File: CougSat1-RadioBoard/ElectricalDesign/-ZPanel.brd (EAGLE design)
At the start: 96 x 96 mm, 46 parts, among them J1 High Gain Antenna, J2 Deployables, J3 High Gain +, J4 ADCS, J5 Flap +X, J6 Flap -X, J7 Flap +Y, J8 Flap -Y, U1 AD7291, U3 AD8515

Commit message: Layout 1.0.2
Ready for RF
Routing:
- net AGND: track 314.9 -> 315.8 mm

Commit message: Laid out RF
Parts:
- moved J6 104.7 mm to (-26.0, 0.00)
- moved J8 104.7 mm to (0.00, -26.0)
- moved J1 69.2 mm to (16.0, -23.3), turned to 90 degrees
- moved C1 68.2 mm to (-42.1, 1.56)
- moved C11 68.2 mm to (-36.0, 11.6)
- moved C12 68.2 mm to (-17.8, 23.6)
- moved C2 68.2 mm to (-35.2, 19.5)
- moved C3 68.2 mm to (-35.9, 15.6)
- moved C4 68.2 mm to (-7.68, 42.0)
- moved C5 68.2 mm to (-17.5, 39.6)
- moved C6 68.2 mm to (-41.7, -5.36)
- moved C7 68.2 mm to (-42.5, 7.64)
- moved C8 68.2 mm to (-42.4, 13.6)
- moved C9 68.2 mm to (-26.2, 26.6)
- moved D1 68.2 mm to (-10.3, 33.5)
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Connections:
- net HIGH_G_1 renamed COAX_CENTER
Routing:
- net SPRING_CONTACT: track 136.1 -> 0.00 mm
- net DEPLOY-H: track 99.0 -> 0.00 mm
- net THERM-5: track 115.6 -> 82.6 mm
- net COAX_CENTER: track 0.00 -> 27.8 mm
- net PGND: track 126.2 -> 106.7 mm, vias 0 -> 1
- net DGND: track 60.5 -> 73.6 mm
- net 3.3V: track 48.1 -> 56.0 mm
- net CHASSIS: track 234.3 -> 236.5 mm
- added copper zone on layer 1, net RFGND
- added copper zone on layer 16, net RFGND
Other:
- outline, holes or cut-outs redrawn

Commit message: Update -ZPanel.brd
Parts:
- moved D1 20.6 mm to (8.72, 25.5), turned to 270 degrees
- moved R11 8.60 mm to (-42.4, 9.45)
- moved RN2 8.06 mm to (15.1, 22.6)
- moved RN1 6.71 mm to (20.2, 39.6)
- moved RT2 6.40 mm to (-30.8, -3.55)
- moved C11 6.32 mm to (-42.0, 13.6)
- moved C9 6.32 mm to (-32.2, 28.6)
- moved C3 6.08 mm to (-41.9, 16.6)
- moved R12 5.39 mm to (-4.17, 31.4), flipped to the bottom, turned to 270 degrees
- moved RT4 5.39 mm to (10.6, 18.4)
- moved U3 5.39 mm to (-15.9, 25.5)
- moved C2 5.10 mm to (-40.2, 20.5)
- moved C12 4.12 mm to (-21.8, 22.6)
- moved R3 4.12 mm to (-22.4, 39.6)
- moved C6 3.55 mm to (-45.0, -4.06)
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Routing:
- net SPRING_CONTACT: track 0.00 -> 125.3 mm, vias 0 -> 2
- net DEPLOY-H: track 0.00 -> 90.4 mm, vias 0 -> 2
- net THERM-5: track 82.6 -> 126.6 mm, vias 2 -> 4
- net I2C_SCL_ADCS: track 0.00 -> 43.8 mm, vias 0 -> 1
- net AVDD: track 68.3 -> 104.8 mm, vias 0 -> 4
- net I2C_SDA_ADCS: track 0.00 -> 34.7 mm, vias 0 -> 1
- net PGND: track 106.7 -> 141.3 mm, vias 1 -> 0
- net AGND: track 315.8 -> 344.7 mm, vias 0 -> 1
- net THERM-6: track 95.0 -> 113.2 mm, vias 2 -> 5
- net THERM-1: track 91.7 -> 109.6 mm, vias 2 -> 4
- net THERM-0: track 94.6 -> 111.7 mm
- net THERM-4: track 72.5 -> 88.1 mm, vias 2 -> 4
- net PHOTODIODE_ADC: track 28.5 -> 41.0 mm
- net AVREF: track 54.0 -> 65.7 mm, vias 2 -> 3
- net THERM-3: track 43.4 -> 53.6 mm, vias 2 -> 1
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
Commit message: Ready for review
Ripped up RF traces
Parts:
- removed J1: High Gain Antenna, CougsInSpace-Connectors:U.FL
- removed J2: Deployables, CougsInSpace-Connectors:PICOLOCK1.5-04
- removed J3: High Gain +, CougsInSpace-Connectors:THT-1.0
- removed J5: Flap +X, CougsInSpace-Connectors:SPRING-0990
- removed J6: Flap -X, CougsInSpace-Connectors:SPRING-0990
- removed J7: Flap +Y, CougsInSpace-Connectors:SPRING-0990
- removed J8: Flap -Y, CougsInSpace-Connectors:SPRING-0990
- removed R1, R2: 15Ω 5%, CougsInSpace-Resistors:THT-15MM
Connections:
- removed net COAX_CENTER: J1.CENTER, J3.1
- removed net DEPLOY-H: J2.1, J2.2, R1.1, R2.1
- removed net RFGND: J1.SHIELD@1, J1.SHIELD@13, J1.SHIELD@2
- removed net SPRING_CONTACT: J2.3, J5.1, J6.1, J7.1, J8.1
- net PGND: no longer J2.4, R1.2, R2.2
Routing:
- net SPRING_CONTACT: track 125.3 -> 0.00 mm, vias 2 -> 0
- net PGND: track 141.3 -> 22.8 mm
- net CHASSIS: track 237.0 -> 330.5 mm
- net DEPLOY-H: track 90.4 -> 0.00 mm, vias 2 -> 0
- net COAX_CENTER: track 27.8 -> 0.00 mm
- removed copper zone on layer 1, net RFGND
- removed copper zone on layer 16, net RFGND

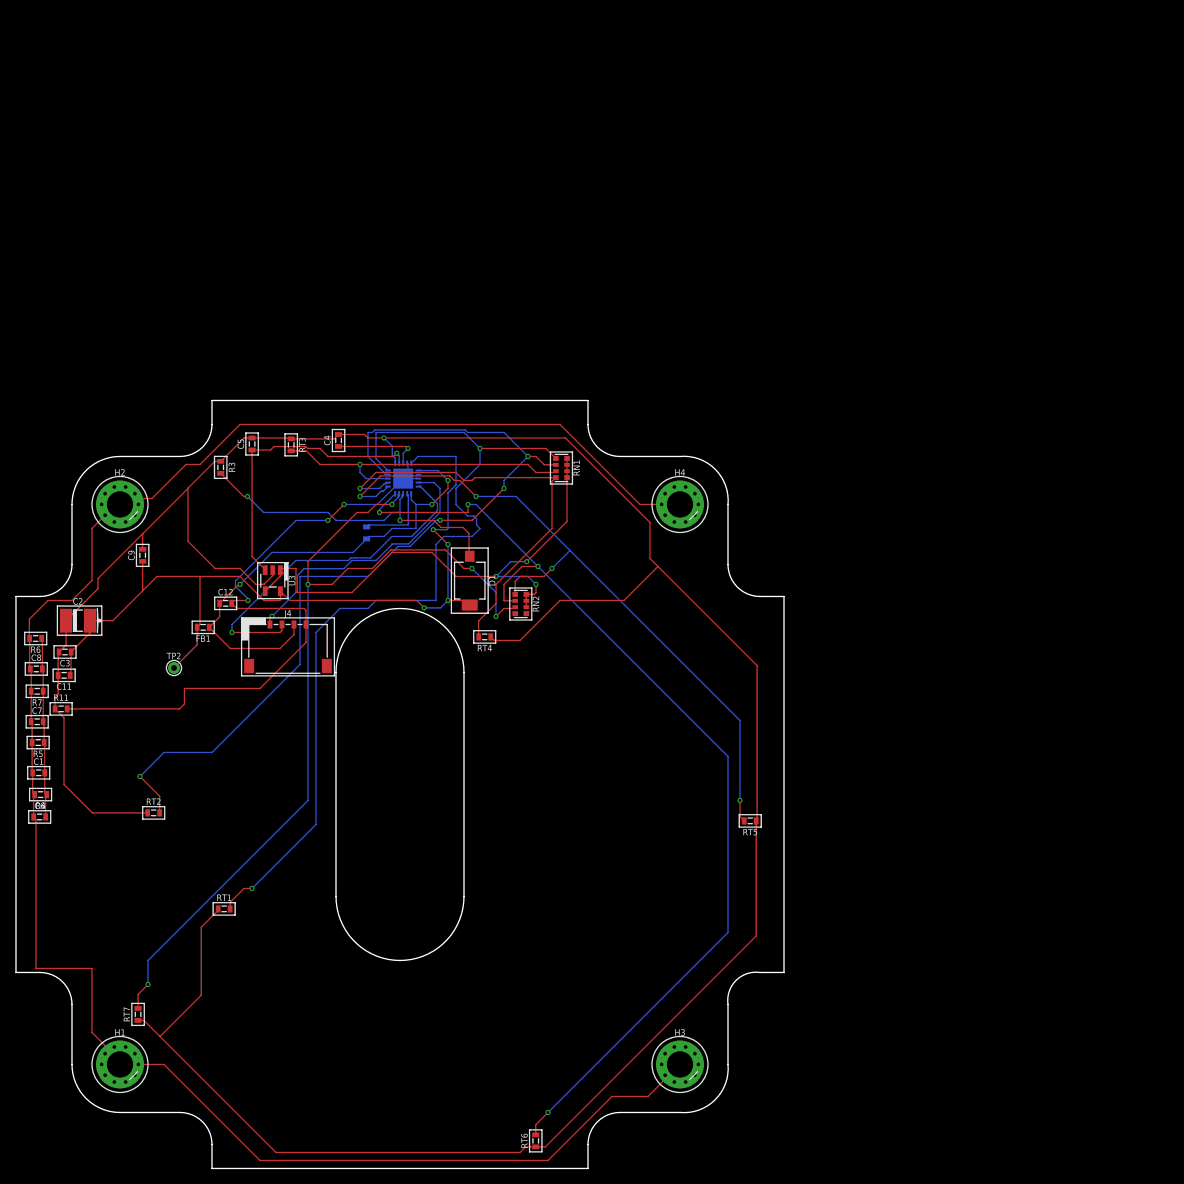
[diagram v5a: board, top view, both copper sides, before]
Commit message: Update -Z Layout
Layout updated considering these notes
- Caps and for chassis should be placed near contacts
- avoid sharp corners
- distance inconsistencies
- top layer components
- snap everything to the grid 0.25mm grid
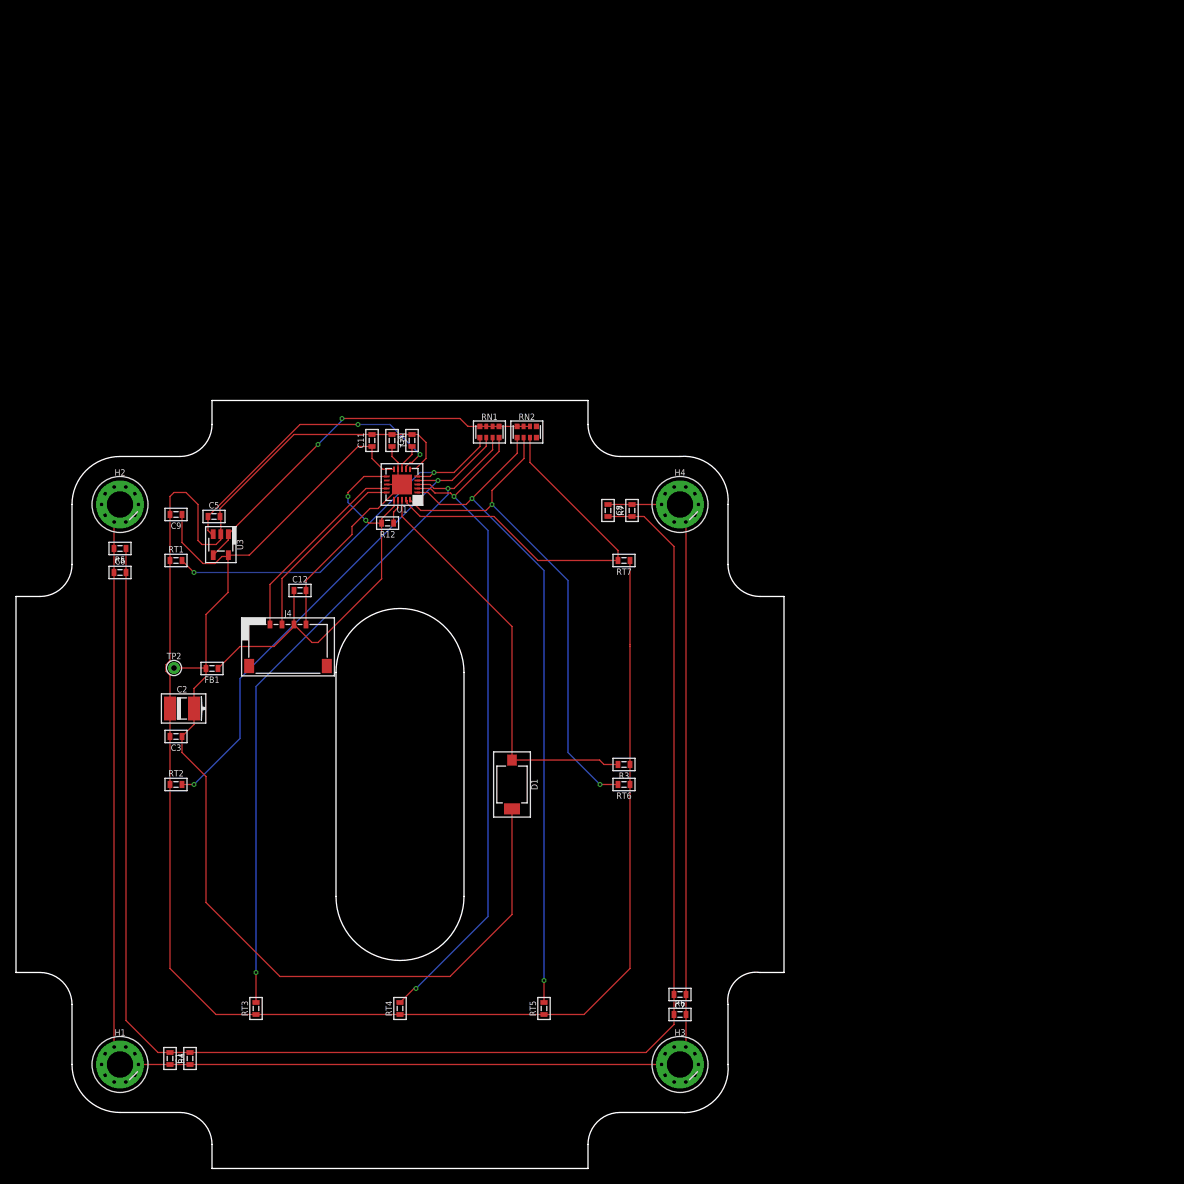
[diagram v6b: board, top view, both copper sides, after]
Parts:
- moved R6 93.3 mm to (35.0, -28.8), turned to 0 degrees
- moved C7 87.3 mm to (35.0, -26.2), turned to 180 degrees
- moved RT7 83.1 mm to (28.0, 28.0), turned to 180 degrees
- moved R7 77.7 mm to (29.0, 34.2), turned to 90 degrees
- moved C8 74.2 mm to (26.0, 34.2), turned to 270 degrees
- moved RT3 70.6 mm to (-18.0, -28.0), turned to 90 degrees
- moved R3 62.6 mm to (28.0, 2.50), turned to 180 degrees
- moved R11 53.3 mm to (-1.00, 43.0), turned to 270 degrees
- moved C11 48.4 mm to (-3.50, 43.0), turned to 90 degrees
- moved RT4 47.6 mm to (0.00, -28.0), turned to 90 degrees
- moved RT6 45.9 mm to (28.0, 0.00), turned to 180 degrees
- moved RT1 44.0 mm to (-28.0, 28.0)
- moved C1 40.4 mm to (-26.2, -34.2), turned to 90 degrees
- moved R4 36.7 mm to (-28.8, -34.2), turned to 270 degrees
- moved RT5 34.8 mm to (18.0, -28.0), turned to 90 degrees
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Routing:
- net PGND: track 22.8 -> 200.2 mm
- net AGND: track 344.7 -> 223.3 mm, vias 1 -> 0
- net THERM-0: track 111.7 -> 47.8 mm
- net THERM-6: track 113.2 -> 49.7 mm, vias 5 -> 0
- net THERM-5: track 126.6 -> 64.0 mm, vias 4 -> 2
- net DGND: track 83.5 -> 30.2 mm, vias 3 -> 0
- net THERM-2: track 39.1 -> 87.4 mm, vias 1 -> 2
- net THERM-1: track 109.6 -> 63.6 mm, vias 4 -> 2
- net AVDD: track 104.9 -> 148.8 mm, vias 4 -> 0
- net THERM-3: track 53.6 -> 84.4 mm, vias 1 -> 2
- net CHASSIS: track 330.5 -> 306.2 mm
- net I2C_SCL_ADCS: track 43.8 -> 23.3 mm, vias 1 -> 0
- net AVREF: track 65.7 -> 47.7 mm, vias 3 -> 2
- net PHOTODIODE_ADC: track 41.0 -> 51.7 mm, vias 2 -> 0
- net I2C_SDA_ADCS: track 34.7 -> 24.6 mm, vias 1 -> 0
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
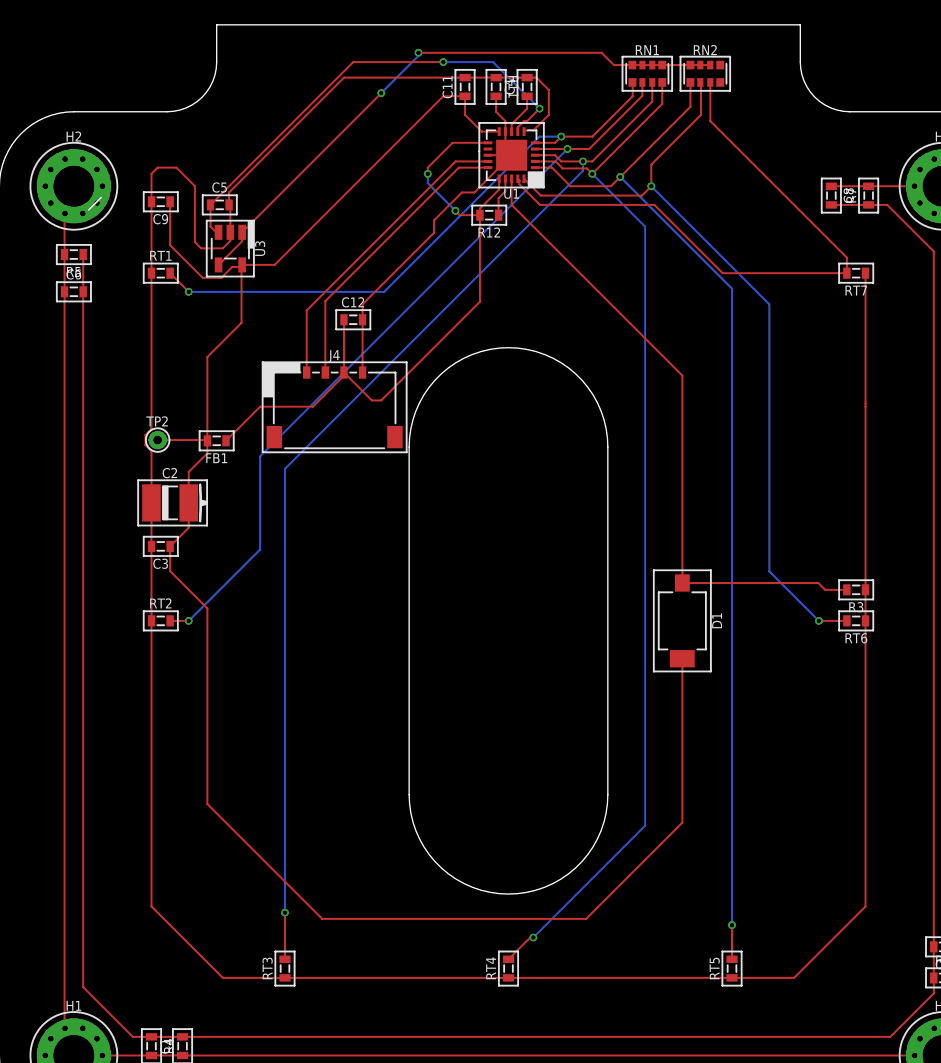
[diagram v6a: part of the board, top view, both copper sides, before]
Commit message: Updated Layout Z
Updated minimizing VREF and adding R1 to connect DGND to PGND
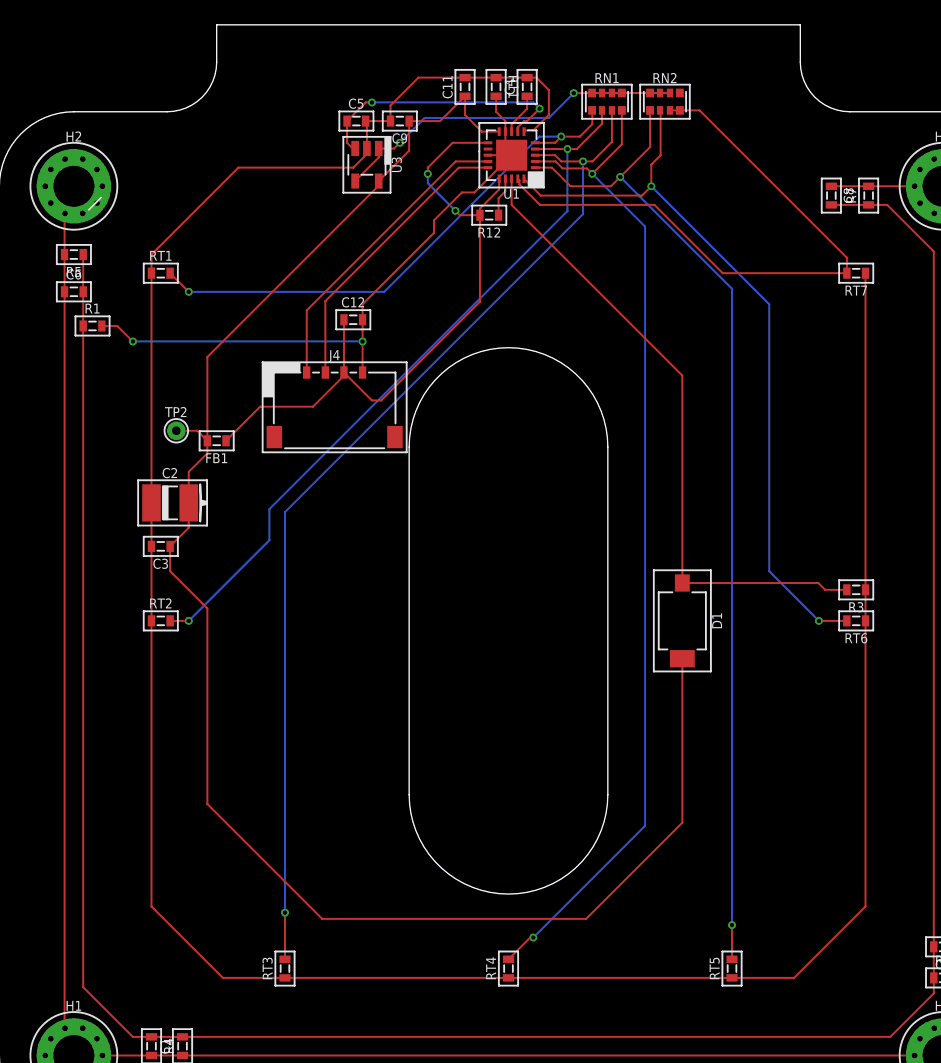
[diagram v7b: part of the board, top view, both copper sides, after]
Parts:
- added R1: 0Ω <20mΩ, CougsInSpace-Resistors:1608
- moved C9 20.3 mm to (-8.75, 40.2)
- moved C5 12.9 mm to (-12.2, 40.2)
- moved U3 12.9 mm to (-11.4, 36.7)
- moved RN1 3.95 mm to (7.93, 41.8)
- moved RN2 3.95 mm to (12.6, 41.8)
- moved TP2 1.68 mm to (-26.8, 15.3)
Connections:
- net DGND: now also R1.2
- net PGND: now also R1.1
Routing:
- net DGND: track 30.2 -> 51.7 mm, vias 0 -> 2
- net AVREF: track 47.7 -> 28.7 mm
- net VREF: track 38.1 -> 21.6 mm
- net AVDD: track 148.8 -> 135.7 mm
- net AGND: track 223.3 -> 211.1 mm
- net THERM-0: track 47.8 -> 43.6 mm
- net THERM-1: track 63.6 -> 59.4 mm
- net THERM-4: track 84.5 -> 80.9 mm
- net THERM-3: track 84.4 -> 80.8 mm
- net THERM-5: track 64.0 -> 60.4 mm
- net THERM-2: track 87.4 -> 83.8 mm
